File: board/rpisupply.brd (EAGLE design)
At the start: 35 x 35 mm, 21 parts, among them IC1 ATTINY45-20SU, Q1 IRF7416, SW1 SCHURTER-LSH-1301.x, X1 MINI-USB, X2 AVR-ISP-6-EDGE

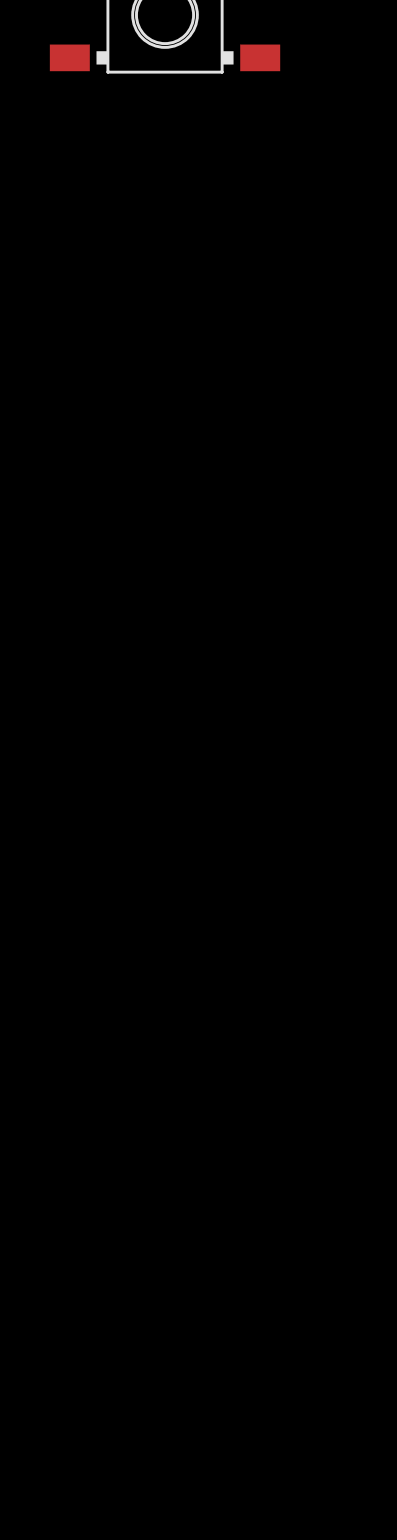
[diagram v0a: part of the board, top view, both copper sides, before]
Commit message: add bidirectional levelshifter
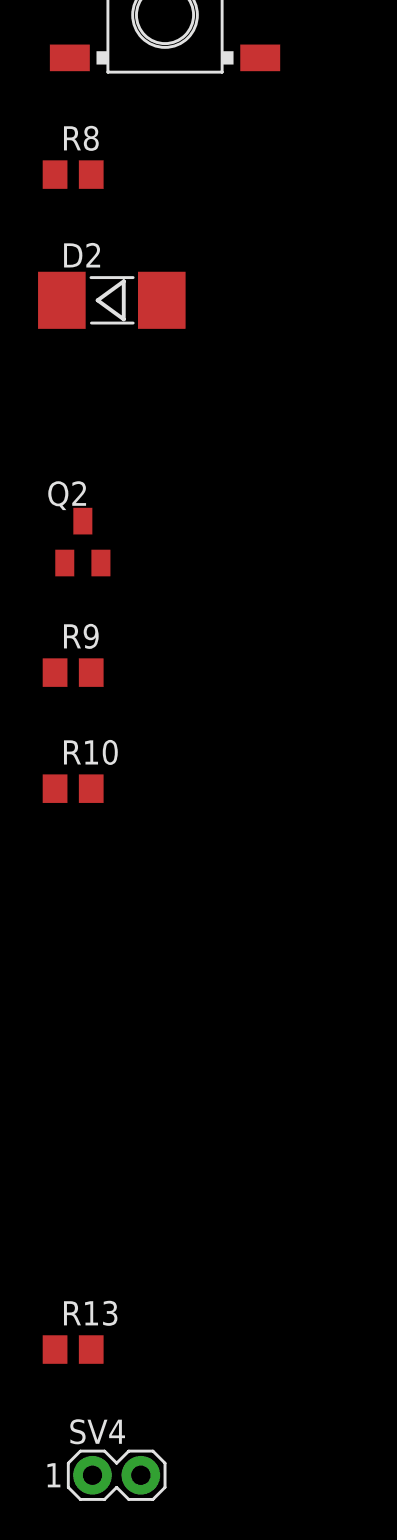
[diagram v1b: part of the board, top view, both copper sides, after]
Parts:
- added D2: 1N4007, diode:MELF-MLL41
- added Q2: BSS138, transistor-fet:SOT23
- added R10, R9: 10k, rcl:R0805
- added R13, R8: 100R, rcl:R0805
- added SV4: (no value), con-lstb:MA02-1
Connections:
- new net N$12: Q2.3, R13.2, R9.2
- new net N$6: Q1.4, R3.2, R8.1
- new net N$7: C1.+, C2.1, D2.C, IC1.8
- new net N$8: Q2.1, R10.1, SV4.1
- new net N$9: Q2.2, R10.2, SV4.2
- net +5V: now also D2.A, R9.1; no longer C1.+, C2.1, IC1.8
- net B3: now also R8.2; no longer Q1.4, R3.2
- net B4: now also R13.1
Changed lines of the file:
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@@
 <?xml version="1.0" encoding="utf-8"?>
 <!DOCTYPE eagle SYSTEM "eagle.dtd">
-<eagle version="6.3">
+<eagle version="7.4.0">
 <drawing>
 <settings>
@@
 <layer number="97" name="Info" color="7" fill="1" visible="no" active="no"/>
 <layer number="98" name="Guide" color="6" fill="1" visible="no" active="no"/>
+<layer number="99" name="SpiceOrder" color="5" fill="1" visible="no" active="no"/>
 <layer number="200" name="200bmp" color="1" fill="10" visible="no" active="no"/>
 </layers>
@@
 <pass name="Default">
 <param name="RoutingGrid" value="50mil"/>
+<param name="AutoGrid" value="1"/>
+<param name="Efforts" value="0"/>
+<param name="TopRouterVariant" value="1"/>
 <param name="tpViaShape" value="round"/>
 <param name="PrefDir.1" value="|"/>
@@
 <element name="X1" library="usb_con-update" package="UX60-MB-5ST" value="MINI-USB" x="5.08" y="6.35"/>
 <element name="SW1" library="_schurter_LPH_LPS_LSH_SMS" package="LSH" value="SCHURTER-LSH-1301.x" x="-46.99" y="-17.018"/>
+<element name="R8" library="rcl" package="R0805" value="100R" x="-51.816" y="-25.4"/>
+<element name="D2" library="diode" package="MELF-MLL41" value="1N4007" x="-49.784" y="-32.004"/>
+<element name="Q2" library="transistor-fet" package="SOT23" value="BSS138" x="-51.308" y="-44.704"/>
+<element name="R9" library="rcl" package="R0805" value="10k" x="-51.816" y="-51.562"/>
+<element name="R10" library="rcl" package="R0805" value="10k" x="-51.816" y="-57.658"/>
+<element name="R13" library="rcl" package="R0805" value="100R" x="-51.816" y="-87.122"/>
+<element name="SV4" library="con-lstb" package="MA02-1" value="" x="-49.53" y="-93.726"/>
 </elements>
 <signals>
@@
 </signal>
 <signal name="+5V">
-<contactref element="C1" pad="+"/>
-<contactref element="C2" pad="1"/>
-<contactref element="IC1" pad="8"/>
 <contactref element="R2" pad="2"/>
 <contactref element="R4" pad="1"/>
@@
 <contactref element="Q1" pad="3"/>
 <contactref element="X1" pad="1"/>
-<wire x1="40.58" y1="28.575" x2="40.58" y2="29.845" width="0" layer="19" extent="1-1"/>
-<wire x1="40.58" y1="27.305" x2="40.58" y2="28.575" width="0" layer="19" extent="1-1"/>
-<wire x1="20.934" y1="10.795" x2="40.58" y2="27.305" width="0" layer="19" extent="1-1"/>
-<wire x1="7.33" y1="7.95" x2="20.934" y2="10.795" width="0" layer="19" extent="1-1"/>
-<wire x1="6.35" y1="-7.62" x2="7.33" y2="7.95" width="0" layer="19" extent="1-1"/>
+<contactref element="D2" pad="A"/>
+<contactref element="R9" pad="1"/>
+<wire x1="-47.159" y1="-32.004" x2="-52.766" y2="-51.562" width="0" layer="19" extent="1-1"/>
+<wire x1="6.35" y1="-7.62" x2="-47.159" y2="-32.004" width="0" layer="19" extent="1-1"/>
 <wire x1="20.955" y1="-9.525" x2="6.35" y2="-7.62" width="0" layer="19" extent="16-16"/>
-<wire x1="-19.01" y1="22.86" x2="7.33" y2="7.95" width="0" layer="19" extent="1-1"/>
-<wire x1="-18.73" y1="27.94" x2="-19.01" y2="22.86" width="0" layer="19" extent="1-1"/>
-<wire x1="-20.64" y1="50.8" x2="-18.73" y2="27.94" width="0" layer="19" extent="1-1"/>
+<wire x1="7.33" y1="7.95" x2="6.35" y2="-7.62" width="0" layer="19" extent="1-1"/>
+<wire x1="40.58" y1="27.305" x2="7.33" y2="7.95" width="0" layer="19" extent="1-1"/>
+<wire x1="40.58" y1="28.575" x2="40.58" y2="27.305" width="0" layer="19" extent="1-1"/>
+<wire x1="40.58" y1="29.845" x2="40.58" y2="28.575" width="0" layer="19" extent="1-1"/>
+<wire x1="-20.64" y1="50.8" x2="7.33" y2="7.95" width="0" layer="19" extent="1-1"/>
 <wire x1="-27.62" y1="50.8" x2="-20.64" y2="50.8" width="0" layer="19" extent="1-1"/>
 <wire x1="-47.94" y1="40.64" x2="-27.62" y2="50.8" width="0" layer="19" extent="1-1"/>
@@
 <contactref element="IC1" pad="3"/>
 <contactref element="R6" pad="2"/>
-<wire x1="14.626" y1="8.265" x2="9.84" y2="27.94" width="0" layer="19" extent="1-1"/>
+<contactref element="R13" pad="1"/>
+<wire x1="14.626" y1="8.265" x2="-52.766" y2="-87.122" width="0" layer="19" extent="1-1"/>
+<wire x1="9.84" y1="27.94" x2="14.626" y2="8.265" width="0" layer="19" extent="1-1"/>
 </signal>
 <signal name="B3">
 <contactref element="IC1" pad="2"/>
-<contactref element="R3" pad="2"/>
-<contactref element="Q1" pad="4"/>
-<wire x1="14.626" y1="9.535" x2="40.58" y2="26.035" width="0" layer="19" extent="1-1"/>
-<wire x1="-25.72" y1="50.8" x2="40.58" y2="26.035" width="0" layer="19" extent="1-1"/>
+<contactref element="R8" pad="2"/>
+<wire x1="14.626" y1="9.535" x2="-50.866" y2="-25.4" width="0" layer="19" extent="1-1"/>
 </signal>
 <signal name="B2">
@@
 <wire x1="-37.78" y1="50.8" x2="-41.99" y2="-14.768" width="0" layer="19" extent="1-1"/>
 </signal>
+<signal name="N$6">
+<contactref element="R8" pad="1"/>
+<contactref element="Q1" pad="4"/>
+<contactref element="R3" pad="2"/>
+<wire x1="-25.72" y1="50.8" x2="-52.766" y2="-25.4" width="0" layer="19" extent="1-1"/>
+<wire x1="40.58" y1="26.035" x2="-25.72" y2="50.8" width="0" layer="19" extent="1-1"/>
+</signal>
+<signal name="N$7">
+<contactref element="C2" pad="1"/>
+<contactref element="D2" pad="C"/>
+<contactref element="C1" pad="+"/>
+<contactref element="IC1" pad="8"/>
+<wire x1="-19.01" y1="22.86" x2="-52.409" y2="-32.004" width="0" layer="19" extent="1-1"/>
+<wire x1="-18.73" y1="27.94" x2="-19.01" y2="22.86" width="0" layer="19" extent="1-1"/>
+<wire x1="20.934" y1="10.795" x2="-19.01" y2="22.86" width="0" layer="19" extent="1-1"/>
+</signal>
+<signal name="N$8">
+<contactref element="Q2" pad="1"/>
+<contactref element="R10" pad="1"/>
+<contactref element="SV4" pad="1"/>
+<wire x1="-52.766" y1="-57.658" x2="-50.8" y2="-93.726" width="0" layer="19" extent="1-1"/>
+<wire x1="-52.258" y1="-45.804" x2="-52.766" y2="-57.658" width="0" layer="19" extent="1-1"/>
+</signal>
+<signal name="N$9">
+<contactref element="Q2" pad="2"/>
+<contactref element="R10" pad="2"/>
+<contactref element="SV4" pad="2"/>
+<wire x1="-50.866" y1="-57.658" x2="-48.26" y2="-93.726" width="0" layer="19" extent="1-1"/>
+<wire x1="-50.358" y1="-45.804" x2="-50.866" y2="-57.658" width="0" layer="19" extent="1-1"/>
+</signal>
+<signal name="N$12">
+<contactref element="Q2" pad="3"/>
+<contactref element="R9" pad="2"/>
+<contactref element="R13" pad="2"/>
+<wire x1="-50.866" y1="-51.562" x2="-50.866" y2="-87.122" width="0" layer="19" extent="1-1"/>
+<wire x1="-51.308" y1="-43.604" x2="-50.866" y2="-51.562" width="0" layer="19" extent="1-1"/>
+</signal>
 </signals>

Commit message: add components for next version
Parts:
- removed SV4: (no value), con-lstb:MA02-1
- added Q3: BSS138, transistor-fet:SOT23
- added Q4: IRF4905S, transistor-fet:D2PACK
- added R11, R12: 10k, rcl:R0805
- added R14: 100R, rcl:R0805
- added SV5: (no value), con-lstb:MA03-1
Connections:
- new net N$10: Q3.3, R11.2, R14.2
- new net N$11: Q3.2, R12.2, SV5.3
- net +5V: now also R11.1
- net B0: now also R13.1
- net B2: now also R14.1
- net B4: no longer R13.1
- net N$8: now also Q3.1, R12.1, SV5.1; no longer SV4.1
- net N$9: now also SV5.2; no longer SV4.2
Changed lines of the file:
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@@
 <element name="R10" library="rcl" package="R0805" value="10k" x="-51.816" y="-57.658"/>
 <element name="R13" library="rcl" package="R0805" value="100R" x="-51.816" y="-87.122"/>
-<element name="SV4" library="con-lstb" package="MA02-1" value="" x="-49.53" y="-93.726"/>
+<element name="SV5" library="con-lstb" package="MA03-1" value="" x="-48.26" y="-98.552">
+<attribute name="MPN" value="" x="-48.26" y="-98.552" size="1.778" layer="27" display="off"/>
+<attribute name="OC_NEWARK" value="unknown" x="-48.26" y="-98.552" size="1.778" layer="27" display="off"/>
+<attribute name="MF" value="" x="-48.26" y="-98.552" size="1.778" layer="27" display="off"/>
+<attribute name="OC_FARNELL" value="unknown" x="-48.26" y="-98.552" size="1.778" layer="27" display="off"/>
+</element>
+<element name="R11" library="rcl" package="R0805" value="10k" x="-51.816" y="-102.87"/>
+<element name="R12" library="rcl" package="R0805" value="10k" x="-51.816" y="-108.966"/>
+<element name="R14" library="rcl" package="R0805" value="100R" x="-51.816" y="-115.062"/>
+<element name="Q3" library="transistor-fet" package="SOT23" value="BSS138" x="-51.308" y="-121.92"/>
+<element name="Q4" library="transistor-fet" package="D2PACK" value="IRF4905S" x="-59.69" y="-114.554"/>
 </elements>
 <signals>
@@
 <contactref element="D2" pad="A"/>
 <contactref element="R9" pad="1"/>
+<contactref element="R11" pad="1"/>
+<wire x1="-52.766" y1="-51.562" x2="-52.766" y2="-102.87" width="0" layer="19" extent="1-1"/>
 <wire x1="-47.159" y1="-32.004" x2="-52.766" y2="-51.562" width="0" layer="19" extent="1-1"/>
 <wire x1="6.35" y1="-7.62" x2="-47.159" y2="-32.004" width="0" layer="19" extent="1-1"/>
@@
 <contactref element="IC1" pad="3"/>
 <contactref element="R6" pad="2"/>
-<contactref element="R13" pad="1"/>
-<wire x1="14.626" y1="8.265" x2="-52.766" y2="-87.122" width="0" layer="19" extent="1-1"/>
-<wire x1="9.84" y1="27.94" x2="14.626" y2="8.265" width="0" layer="19" extent="1-1"/>
+<wire x1="14.626" y1="8.265" x2="9.84" y2="27.94" width="0" layer="19" extent="1-1"/>
 </signal>
 <signal name="B3">
@@
 <contactref element="X2" pad="SCK"/>
 <contactref element="LED1" pad="C"/>
-<wire x1="18.415" y1="-9.525" x2="20.934" y2="9.525" width="0" layer="19" extent="1-1"/>
+<contactref element="R14" pad="1"/>
+<wire x1="18.415" y1="-9.525" x2="-52.766" y2="-115.062" width="0" layer="19" extent="1-1"/>
+<wire x1="20.934" y1="9.525" x2="18.415" y2="-9.525" width="0" layer="19" extent="1-1"/>
 <wire x1="-41.69" y1="38.1" x2="20.934" y2="9.525" width="0" layer="19" extent="1-1"/>
 </signal>
@@
 <contactref element="X2" pad="MOSI"/>
 <contactref element="R5" pad="2"/>
-<wire x1="18.415" y1="-9.525" x2="20.934" y2="6.985" width="0" layer="19" extent="1-16"/>
+<contactref element="R13" pad="1"/>
+<wire x1="18.415" y1="-9.525" x2="-52.766" y2="-87.122" width="0" layer="19" extent="1-16"/>
+<wire x1="20.934" y1="6.985" x2="18.415" y2="-9.525" width="0" layer="19" extent="1-16"/>
 <wire x1="-35.88" y1="50.8" x2="20.934" y2="6.985" width="0" layer="19" extent="1-1"/>
 </signal>
@@
 <contactref element="Q2" pad="1"/>
 <contactref element="R10" pad="1"/>
-<contactref element="SV4" pad="1"/>
-<wire x1="-52.766" y1="-57.658" x2="-50.8" y2="-93.726" width="0" layer="19" extent="1-1"/>
+<contactref element="SV5" pad="1"/>
+<contactref element="R12" pad="1"/>
+<contactref element="Q3" pad="1"/>
+<wire x1="-52.766" y1="-108.966" x2="-52.258" y2="-123.02" width="0" layer="19" extent="1-1"/>
+<wire x1="-50.8" y1="-98.552" x2="-52.766" y2="-108.966" width="0" layer="19" extent="1-1"/>
+<wire x1="-52.766" y1="-57.658" x2="-50.8" y2="-98.552" width="0" layer="19" extent="1-1"/>
 <wire x1="-52.258" y1="-45.804" x2="-52.766" y2="-57.658" width="0" layer="19" extent="1-1"/>
 </signal>
+<signal name="N$12">
+<contactref element="R9" pad="2"/>
+<contactref element="R13" pad="2"/>
+<contactref element="Q2" pad="3"/>
+<wire x1="-50.866" y1="-51.562" x2="-50.866" y2="-87.122" width="0" layer="19" extent="1-1"/>
+<wire x1="-51.308" y1="-43.604" x2="-50.866" y2="-51.562" width="0" layer="19" extent="1-1"/>
+</signal>
 <signal name="N$9">
+<contactref element="SV5" pad="2"/>
 <contactref element="Q2" pad="2"/>
 <contactref element="R10" pad="2"/>
-<contactref element="SV4" pad="2"/>
-<wire x1="-50.866" y1="-57.658" x2="-48.26" y2="-93.726" width="0" layer="19" extent="1-1"/>
+<wire x1="-50.866" y1="-57.658" x2="-48.26" y2="-98.552" width="0" layer="19" extent="1-1"/>
 <wire x1="-50.358" y1="-45.804" x2="-50.866" y2="-57.658" width="0" layer="19" extent="1-1"/>
 </signal>
-<signal name="N$12">
-<contactref element="Q2" pad="3"/>
-<contactref element="R9" pad="2"/>
-<contactref element="R13" pad="2"/>
-<wire x1="-50.866" y1="-51.562" x2="-50.866" y2="-87.122" width="0" layer="19" extent="1-1"/>
-<wire x1="-51.308" y1="-43.604" x2="-50.866" y2="-51.562" width="0" layer="19" extent="1-1"/>
+<signal name="N$10">
+<contactref element="R11" pad="2"/>
+<contactref element="R14" pad="2"/>
+<contactref element="Q3" pad="3"/>
+<wire x1="-50.866" y1="-115.062" x2="-51.308" y2="-120.82" width="0" layer="19" extent="1-1"/>
+<wire x1="-50.866" y1="-102.87" x2="-50.866" y2="-115.062" width="0" layer="19" extent="1-1"/>
+</signal>
+<signal name="N$11">
+<contactref element="R12" pad="2"/>
+<contactref element="Q3" pad="2"/>
+<contactref element="SV5" pad="3"/>
+<wire x1="-50.866" y1="-108.966" x2="-50.358" y2="-123.02" width="0" layer="19" extent="1-1"/>
+<wire x1="-45.72" y1="-98.552" x2="-50.866" y2="-108.966" width="0" layer="19" extent="1-1"/>
 </signal>
 </signals>

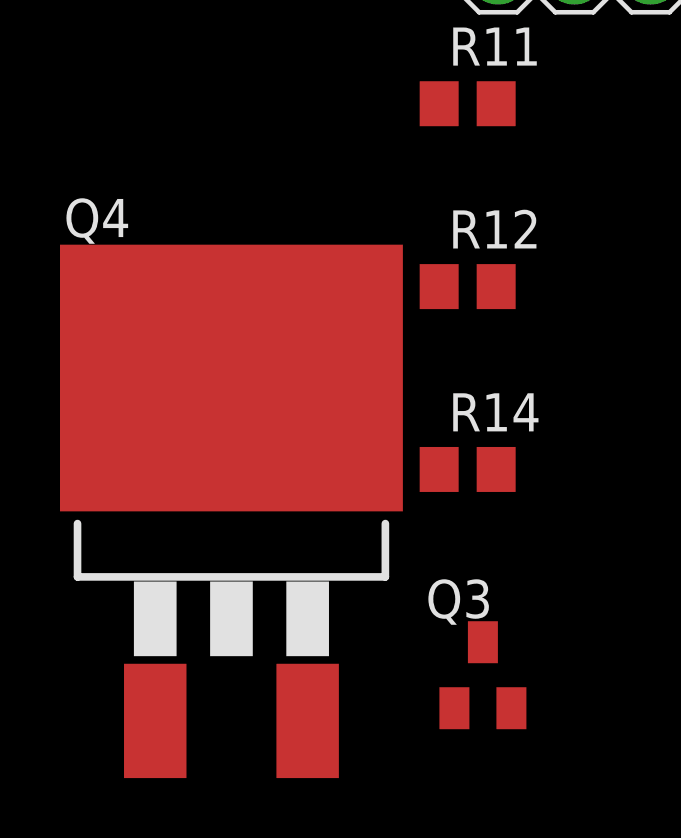
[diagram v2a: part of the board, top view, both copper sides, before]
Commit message: change docs to mkdocs
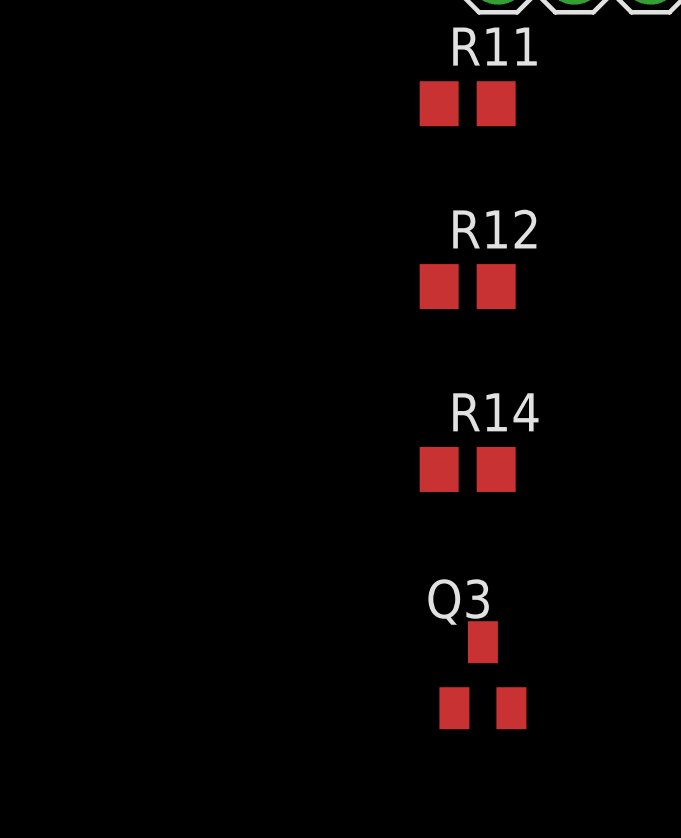
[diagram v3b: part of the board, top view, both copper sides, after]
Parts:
- removed Q4: IRF4905S, transistor-fet:D2PACK
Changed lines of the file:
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@@
 <?xml version="1.0" encoding="utf-8"?>
 <!DOCTYPE eagle SYSTEM "eagle.dtd">
-<eagle version="7.4.0">
+<eagle version="7.5.0">
 <drawing>
 <settings>
@@
 <element name="R14" library="rcl" package="R0805" value="100R" x="-51.816" y="-115.062"/>
 <element name="Q3" library="transistor-fet" package="SOT23" value="BSS138" x="-51.308" y="-121.92"/>
-<element name="Q4" library="transistor-fet" package="D2PACK" value="IRF4905S" x="-59.69" y="-114.554"/>
 </elements>
 <signals>
